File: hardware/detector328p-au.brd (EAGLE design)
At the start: 57 x 88 mm, 65 parts, among them J1 AVR_SPI_PRG_6NS, K1 SRD-05VDC-SL-C, Q1 BSS123, Q2 16MHz, T1 BC817-40SMD, T2 BC817, T3 BC817, U1 ATMEGA328P-AU

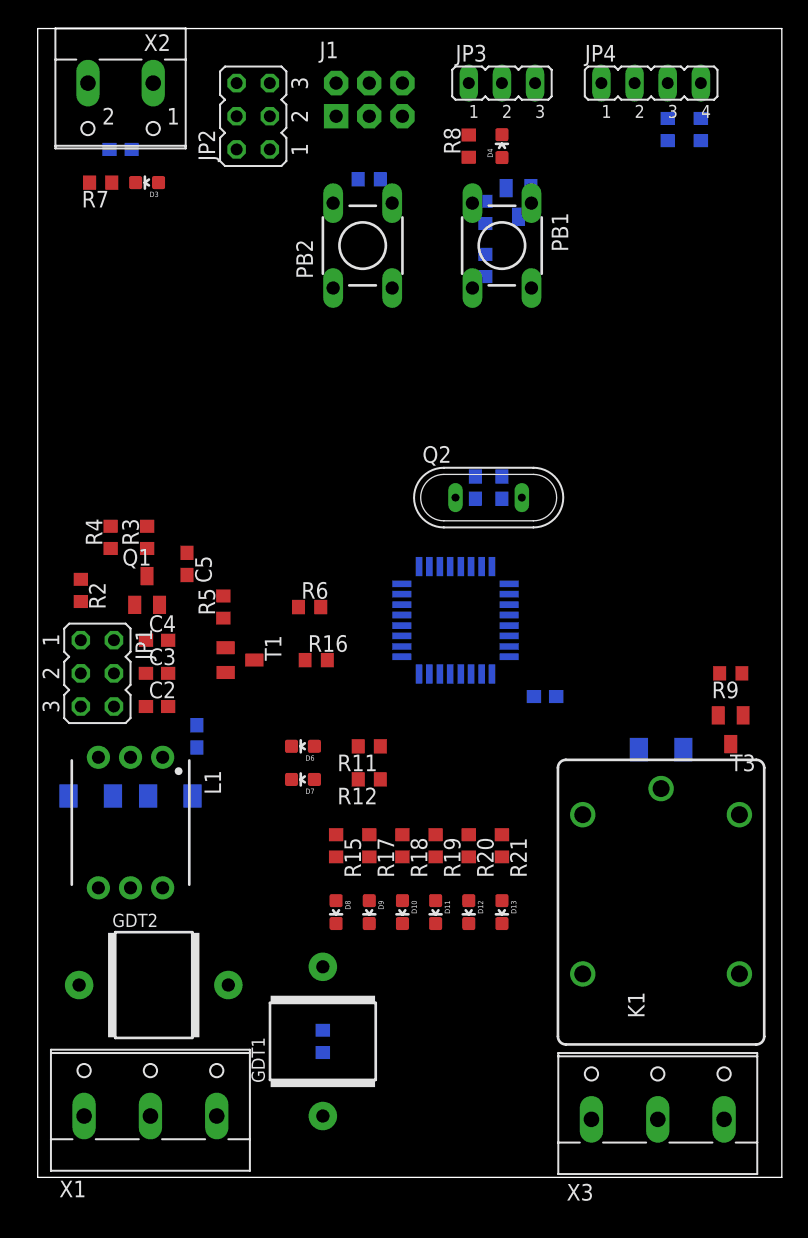
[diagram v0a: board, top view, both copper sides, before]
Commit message: detector328p-au level 1: devices at place
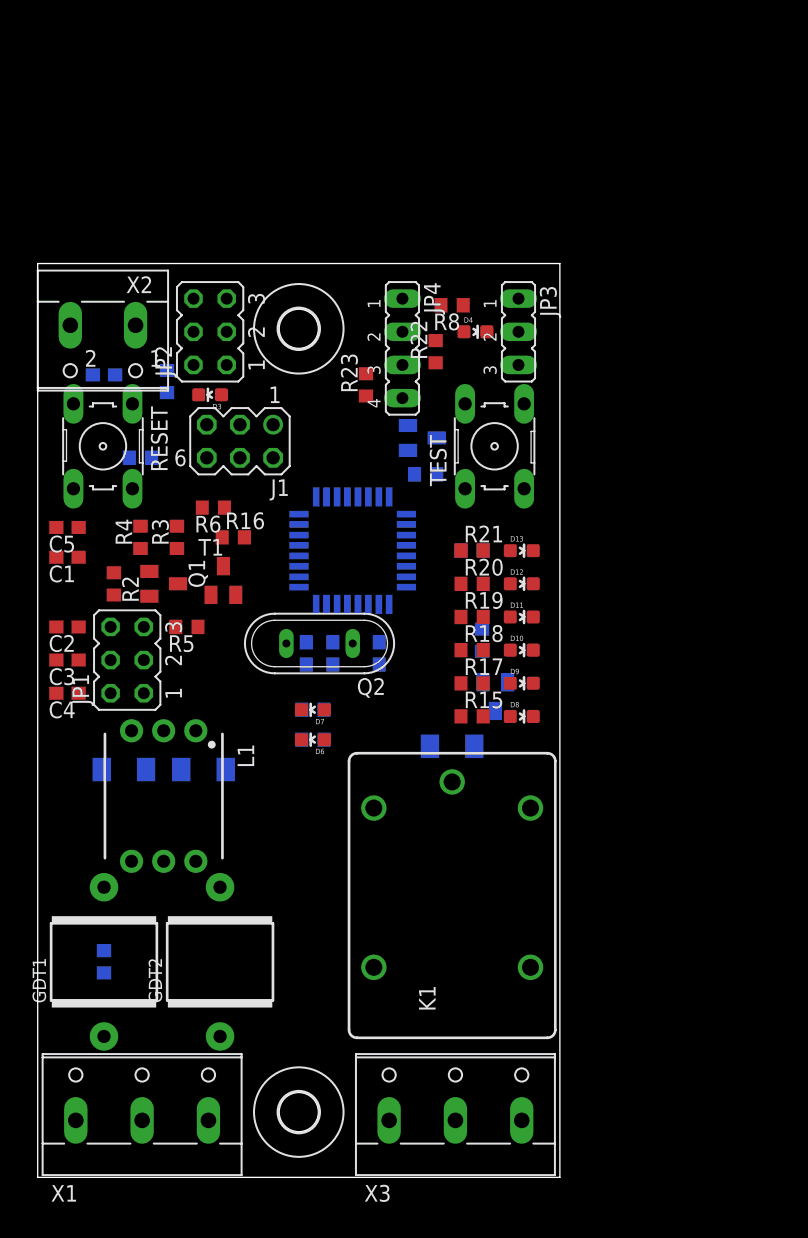
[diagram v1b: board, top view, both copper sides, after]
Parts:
- removed PB1, PB2: TACTILE-SWITCH-PTH, GeekAmmo:TAC-SWITCH-PTH
- added RESET, TEST: (no value), detector:B3F-10XX
- added U$1, U$2: (no value), holes:3,0
- J1: value AVR_SPI_PRG_6NS -> (none); device SparkFun-Connectors:2X3-NS -> con-lstb:MA03-2
- moved R23 32.3 mm to (25.1, 60.7), flipped to the top, turned to 90 degrees
- moved J1 28.0 mm to (15.5, 56.4), turned to 180 degrees
- moved JP4 27.9 mm to (27.9, 63.5), turned to 270 degrees
- moved D13 27.7 mm to (37.1, 48.0), turned to 270 degrees
- moved R14 27.6 mm to (7.87, 55.1)
- moved D12 25.5 mm to (37.1, 45.5), turned to 270 degrees
- moved R22 24.6 mm to (30.5, 63.2), flipped to the top, turned to 90 degrees
- moved D11 23.6 mm to (37.1, 42.9), turned to 270 degrees
- moved R21 22.7 mm to (33.3, 48.0), turned to 0 degrees
- moved D10 22.1 mm to (37.1, 40.4), turned to 270 degrees
- moved R13 21.9 mm to (33.3, 48.0), turned to 180 degrees
- moved D9 21.1 mm to (37.1, 37.8), turned to 270 degrees
- moved D8 20.7 mm to (37.1, 35.3), turned to 270 degrees
- moved R10 20.6 mm to (29.7, 53.8), turned to 0 degrees
- moved R20 20.1 mm to (33.3, 45.5), turned to 0 degrees
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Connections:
- net GND: now also JP3.1, RESET.3, RESET.4; no longer JP3.3, PB2.3
- net N$30: now also RESET.1, RESET.2; no longer PB2.1
- net N$47: now also TEST.1, TEST.2; no longer PB1.1
- net VCC: now also JP3.3, TEST.3, TEST.4; no longer JP3.1, PB1.3
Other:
- board size 57 x 88 mm -> 40 x 70 mm

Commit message: detector328p-au almost wired
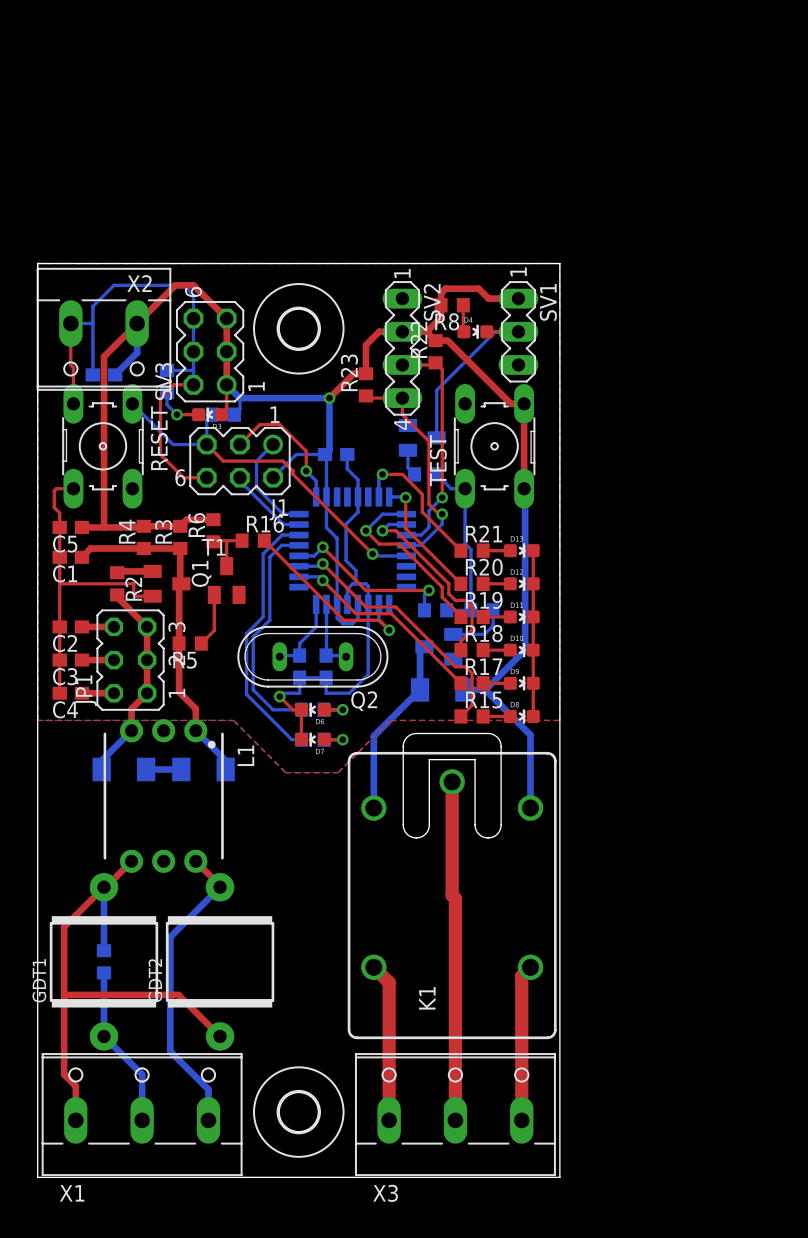
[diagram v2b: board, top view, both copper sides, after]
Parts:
- removed JP2: (no value), jumper:JP3Q
- removed JP3: (no value), jumper:JP2
- removed JP4: (no value), jumper:JP4
- added SV1: (no value), con-lstb:MA03-1
- added SV2: (no value), con-lstb:MA04-1
- added SV3: (no value), con-lstb:MA03-2
- JP1: device jumper:JP3Q -> detector:JP3Q
- X1, X3: device con-wago-508:W237-133 -> detector:W237-3E
- X2: device con-wago-500:W237-102 -> detector:W237-132
- moved C9 15.6 mm to (22.9, 55.4), turned to 180 degrees
- moved R14 7.16 mm to (14.2, 58.4), turned to 180 degrees
- moved T3 5.76 mm to (30.7, 40.6), turned to 270 degrees
- moved R13 5.36 mm to (30.5, 43.4)
- moved D5 4.38 mm to (31.0, 37.3), turned to 0 degrees
- moved D6 2.29 mm to (21.1, 35.8)
- moved D7 2.29 mm to (21.1, 33.5)
- moved R11 2.29 mm to (21.1, 35.8)
- moved R12 2.29 mm to (21.1, 33.5)
- moved R9 2.29 mm to (34.0, 43.4), turned to 0 degrees
- moved R6 1.78 mm to (13.5, 49.5), turned to 90 degrees
- moved R16 1.55 mm to (16.5, 48.8)
- moved D3 1.52 mm to (13.2, 58.4)
- moved J1 1.52 mm to (15.5, 54.9)
- moved R5 1.30 mm to (11.7, 40.9)
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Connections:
- removed net N$39: D5.A, K1.2, T3.C
- new net N$38: D5.A, K1.1, T3.C
- net GND: now also SV1.3, SV2.1, SV3.2, SV3.4, SV3.6; no longer JP2.2, JP2.4, JP2.6, JP3.1, JP4.1
- net N$23: now also SV1.2; no longer JP3.2
- net N$44: now also SV2.4; no longer JP4.4
- net N$45: now also SV2.3; no longer JP4.3
- net VCC: now also K1.2, SV1.1, SV2.2, SV3.1, SV3.3, SV3.5; no longer JP2.1, JP2.3, JP2.5, JP3.3, JP4.2, K1.1
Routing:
- net VCC: track 0.00 -> 149.3 mm, vias 0 -> 1
- net GND: track 0.00 -> 115.2 mm, vias 0 -> 1
- net N$21: track 0.00 -> 40.5 mm
- net N$30: track 0.00 -> 28.4 mm, vias 0 -> 1
- net N$14: track 0.00 -> 26.3 mm
- net N$43: track 0.00 -> 26.0 mm
- net N$7: track 0.00 -> 23.4 mm
- net N$26: track 0.00 -> 20.5 mm, vias 0 -> 1
- net N$36: track 0.00 -> 20.3 mm
- net N$45: track 0.00 -> 17.8 mm, vias 0 -> 1
- net N$37: track 0.00 -> 17.7 mm
- net N$44: track 0.00 -> 17.3 mm, vias 0 -> 1
- net N$25: track 0.00 -> 15.8 mm, vias 0 -> 1
- net N$6: track 0.00 -> 15.8 mm
- net N$28: track 0.00 -> 15.4 mm, vias 0 -> 1
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- added copper zone on layer 1, net GND
- added copper zone on layer 16, net GND
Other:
- outline, holes or cut-outs redrawn

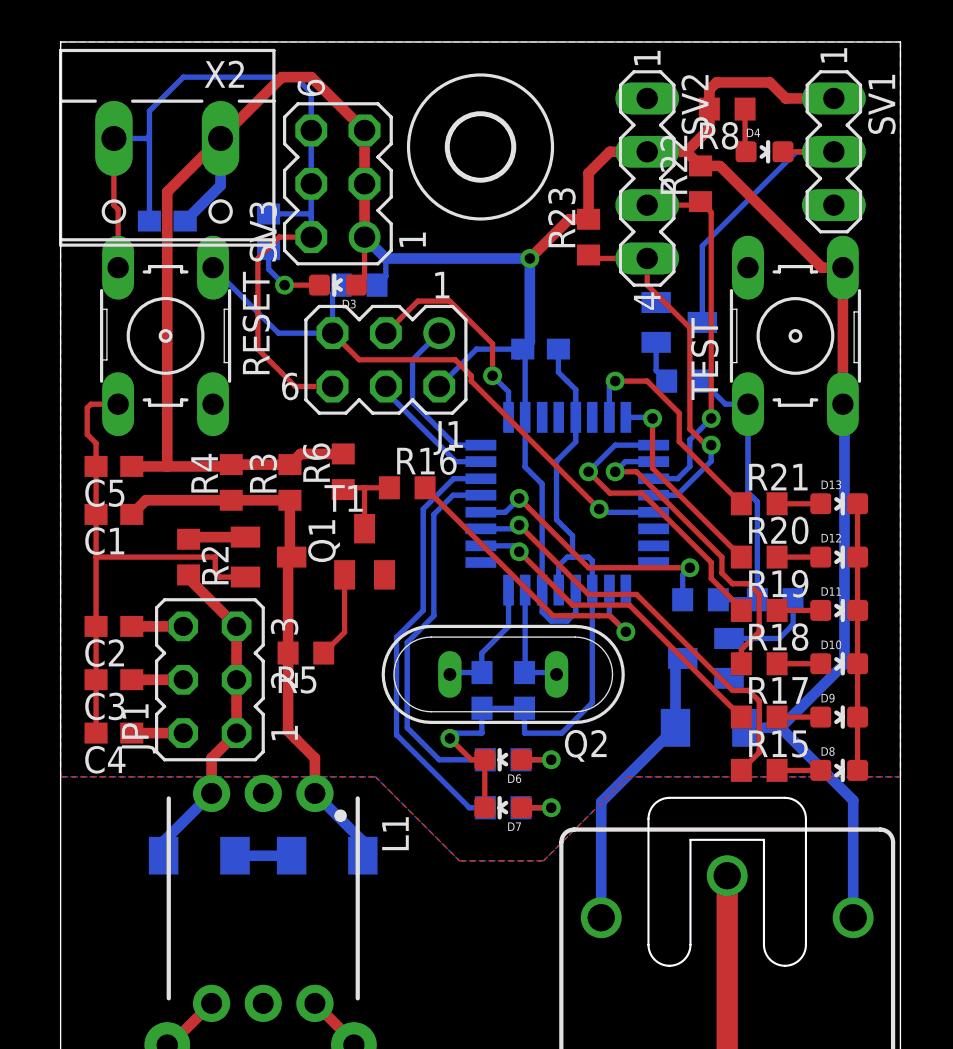
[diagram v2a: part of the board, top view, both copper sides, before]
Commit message: detector328p-au wiring ready, labels need fixing
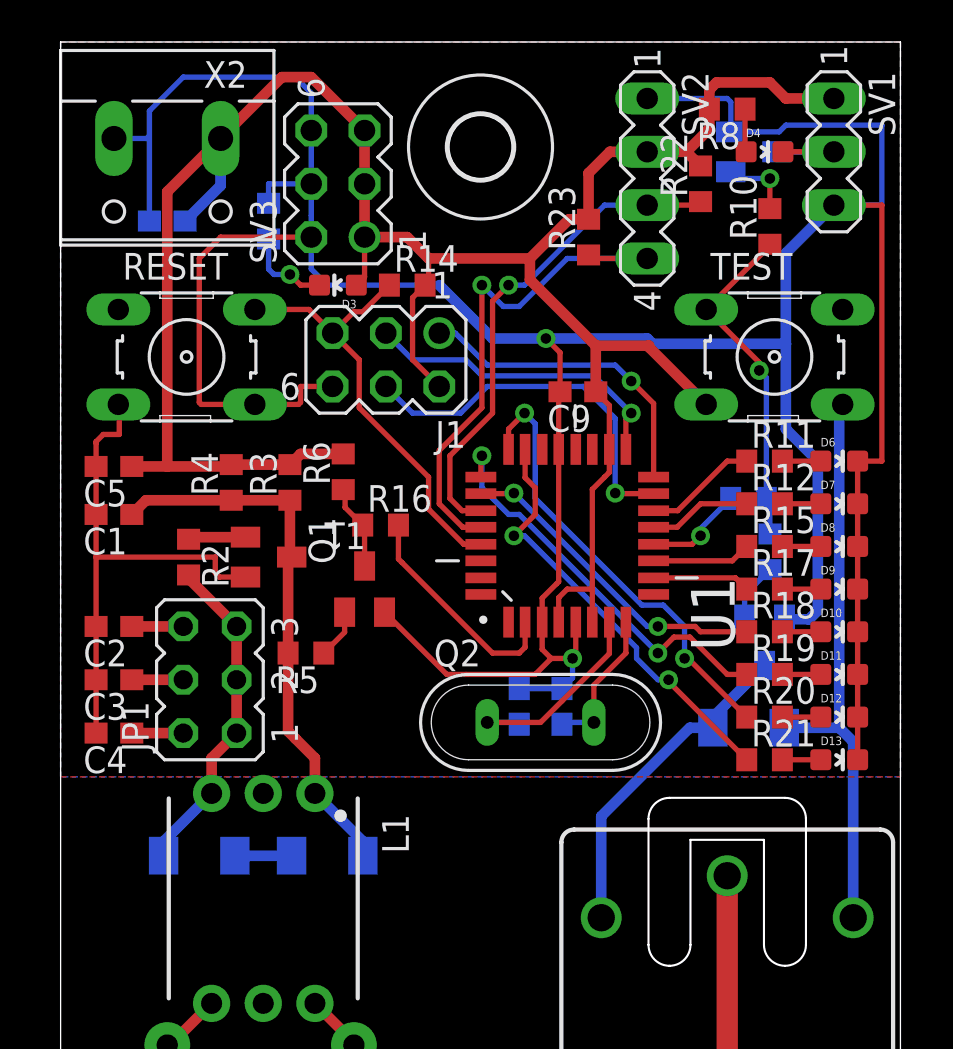
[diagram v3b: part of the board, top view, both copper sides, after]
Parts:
- moved D7 21.6 mm to (37.1, 48.0), turned to 270 degrees
- moved D6 21.4 mm to (37.1, 50.0), turned to 270 degrees
- moved R12 19.1 mm to (33.5, 48.0), flipped to the top, turned to 0 degrees
- moved R11 18.9 mm to (33.5, 50.0), flipped to the top, turned to 0 degrees
- moved R21 12.2 mm to (33.5, 35.8)
- moved D13 12.2 mm to (37.1, 35.8)
- moved R15 10.7 mm to (33.5, 46.0)
- moved D8 10.7 mm to (37.1, 46.0)
- moved T2 8.87 mm to (33.0, 64.8)
- moved R10 8.41 mm to (33.8, 61.2), flipped to the top, turned to 90 degrees
- moved R20 7.62 mm to (33.5, 37.8)
- moved D12 7.62 mm to (37.1, 37.8)
- moved R17 6.10 mm to (33.5, 43.9)
- moved D9 6.10 mm to (37.1, 43.9)
- moved R13 5.34 mm to (32.8, 48.3)
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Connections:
- net N$36: now also R11.1; no longer R12.1
- net N$37: now also R12.1; no longer R11.1
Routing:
- net GND: track 115.2 -> 198.8 mm, vias 1 -> 2
- net N$26: track 20.5 -> 4.72 mm, vias 1 -> 0
- net N$36: track 20.3 -> 5.41 mm
- net N$37: track 17.7 -> 4.90 mm
- net N$31: track 9.65 -> 21.6 mm, vias 1 -> 2
- net N$13: track 6.15 -> 18.0 mm, vias 0 -> 1
- net N$25: track 15.8 -> 4.65 mm, vias 1 -> 0
- net N$33: track 11.1 -> 20.6 mm, vias 1 -> 2
- net N$23: track 14.2 -> 5.13 mm
- net N$46: track 13.3 -> 4.78 mm, vias 2 -> 1
- net N$44: track 17.3 -> 25.8 mm
- net VCC: track 149.3 -> 141.2 mm, vias 1 -> 0
- net N$12: track 7.92 -> 15.1 mm, vias 0 -> 1
- net N$30: track 28.4 -> 21.3 mm, vias 1 -> 0
- net N$45: track 17.8 -> 23.8 mm
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
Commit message: detector328p-au final
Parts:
- moved R3 1.02 mm to (9.91, 49.0)
- moved R6 0.57 mm to (13.2, 49.0), turned to 180 degrees
- moved R16 0.25 mm to (15.0, 47.0)
- moved T1 0.25 mm to (14.2, 43.9)
- renumbered SV1 to OUT, SV2 to LCD, SV3 to POWER
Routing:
- net VCC: track 141.2 -> 140.5 mm
- net GND: track 198.8 -> 199.4 mm
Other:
- board text added: "Car Detector v1.0"

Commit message: detector328p-au serial port
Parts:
- added SERIAL: (no value), con-lstb:MA03-1
- moved R5 7.13 mm to (11.2, 48.0)
- moved R6 2.27 mm to (11.2, 50.0)
- moved R4 2.03 mm to (6.10, 49.0)
- moved R3 1.78 mm to (8.13, 49.0)
- moved T1 1.55 mm to (14.0, 45.5), turned to 270 degrees
- moved R16 1.05 mm to (14.7, 48.0)
- moved C7 0.76 mm to (22.6, 38.4)
- moved C8 0.76 mm to (24.6, 38.4)
- moved Q2 0.76 mm to (23.6, 37.6)
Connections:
- new net N$39: SERIAL.1, U1.30
- new net N$48: SERIAL.3, U1.31
- net GND: now also SERIAL.2
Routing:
- net N$48: track 0.00 -> 10.0 mm, vias 0 -> 1
- net GND: track 199.4 -> 205.9 mm
- net N$39: track 0.00 -> 6.03 mm, vias 0 -> 1
- net VCC: track 140.5 -> 138.1 mm
- net FREQ: track 4.05 -> 5.83 mm
- net N$9: track 11.1 -> 12.6 mm
- net N$8: track 10.1 -> 9.38 mm

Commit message: detector328p-au R2->1K, T1->BC817
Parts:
- R2: value 470 -> 1K
- T1: value BC817-40SMD -> BC817
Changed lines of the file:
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@@
 <attribute name="VALUE" x="32.893" y="37.973" size="1.27" layer="27"/>
 </element>
-<element name="R2" library="resistor" package="R0603" value="470" x="6.096" y="45.466" smashed="yes" rot="R270">
+<element name="R2" library="resistor" package="R0603" value="1K" x="6.096" y="45.466" smashed="yes" rot="R270">
 <attribute name="NAME" x="3.937" y="45.085" size="0.8128" layer="25" font="vector"/>
 <attribute name="VALUE" x="4.191" y="46.101" size="1.27" layer="27" rot="R270"/>
@@
 <attribute name="VALUE" x="31.877" y="45.085" size="1.27" layer="28" rot="MR90"/>
 </element>
-<element name="T1" library="transistor-npn" package="SOT23-BEC" value="BC817-40SMD" x="13.97" y="45.466" smashed="yes" rot="R270">
+<element name="T1" library="transistor-npn" package="SOT23-BEC" value="BC817" x="13.97" y="45.466" smashed="yes" rot="R270">
 <attribute name="NAME" x="16.129" y="45.339" size="0.8128" layer="25" font="vector"/>
 <attribute name="VALUE" x="10.795" y="47.371" size="1.27" layer="27" rot="R270"/>
